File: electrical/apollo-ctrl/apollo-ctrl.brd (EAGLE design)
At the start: 100 x 80 mm, 65 parts, among them Q1 N-chan, Q2 N-chan, U1 NANO, U2 ADAFRUIT-MPRLS, X1 BARREL-JACK, X2 SENSOR-O2, X4 FAN

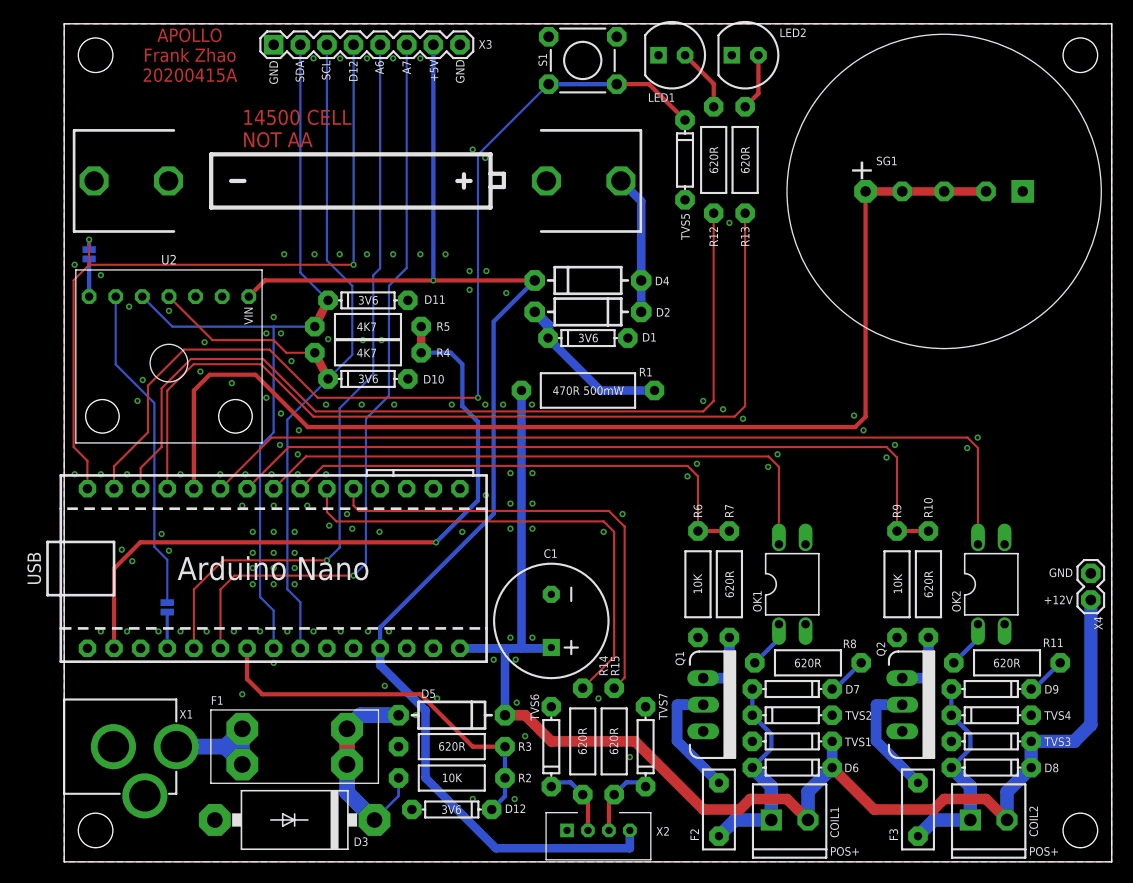
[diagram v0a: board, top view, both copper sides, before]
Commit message: ctrl pcb, more silk text, added extra ADC pins
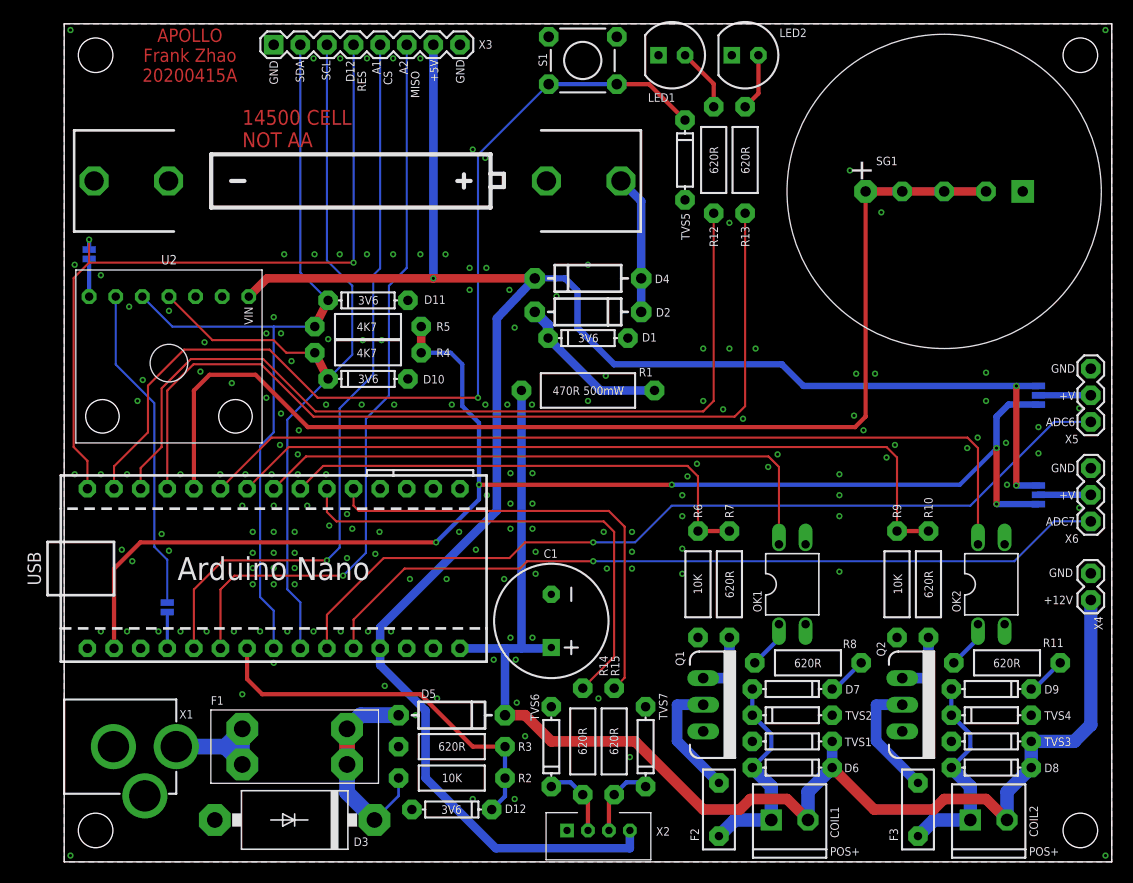
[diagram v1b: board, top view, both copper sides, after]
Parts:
- added SJ3, SJ4: (no value), apollo-ctrl:SJ_3
- added X5, X6: (no value), apollo-ctrl:1X03
- moved D4 0.20 mm to (50.0, 55.7)
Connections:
- new net A6: U1.A6, X5.1
- new net A7: U1.A7, X6.1
- new net N$21: SJ4.2, X6.2
- new net N$22: SJ3.2, X5.2
- net 3.3V: now also SJ3.3, SJ4.3
- net 5V: now also SJ3.1, SJ4.1
- net GND: now also X5.3, X6.3
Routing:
- net A6: track 0.00 -> 83.7 mm, vias 0 -> 1
- net A7: track 0.00 -> 77.0 mm, vias 0 -> 1
- net 3.3V: track 65.5 -> 133.3 mm, vias 1 -> 5
- net 5V: track 129.8 -> 195.8 mm, vias 1 -> 3
- net N$22: track 0.00 -> 5.00 mm
- net N$21: track 0.00 -> 5.00 mm
- net AUX3: track 71.6 -> 71.1 mm
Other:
- board text added: "+3V3"
- board text added: "+V"
- board text added: "A1"
- board text added: "A2"
- board text added: "ADC6"
- board text added: "ADC7"
- board text added: "CS"
- board text added: "MISO"
- board text added: "RES"
- board text removed: "A6"
- board text removed: "A7"
